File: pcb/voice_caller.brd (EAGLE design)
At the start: 52.4 x 59.1 mm, 36 parts, among them IC1 PRO_MICRO, IC3 78L12SMD, K1 TQ2SA-L2-5V, U1 25F32006WSOI

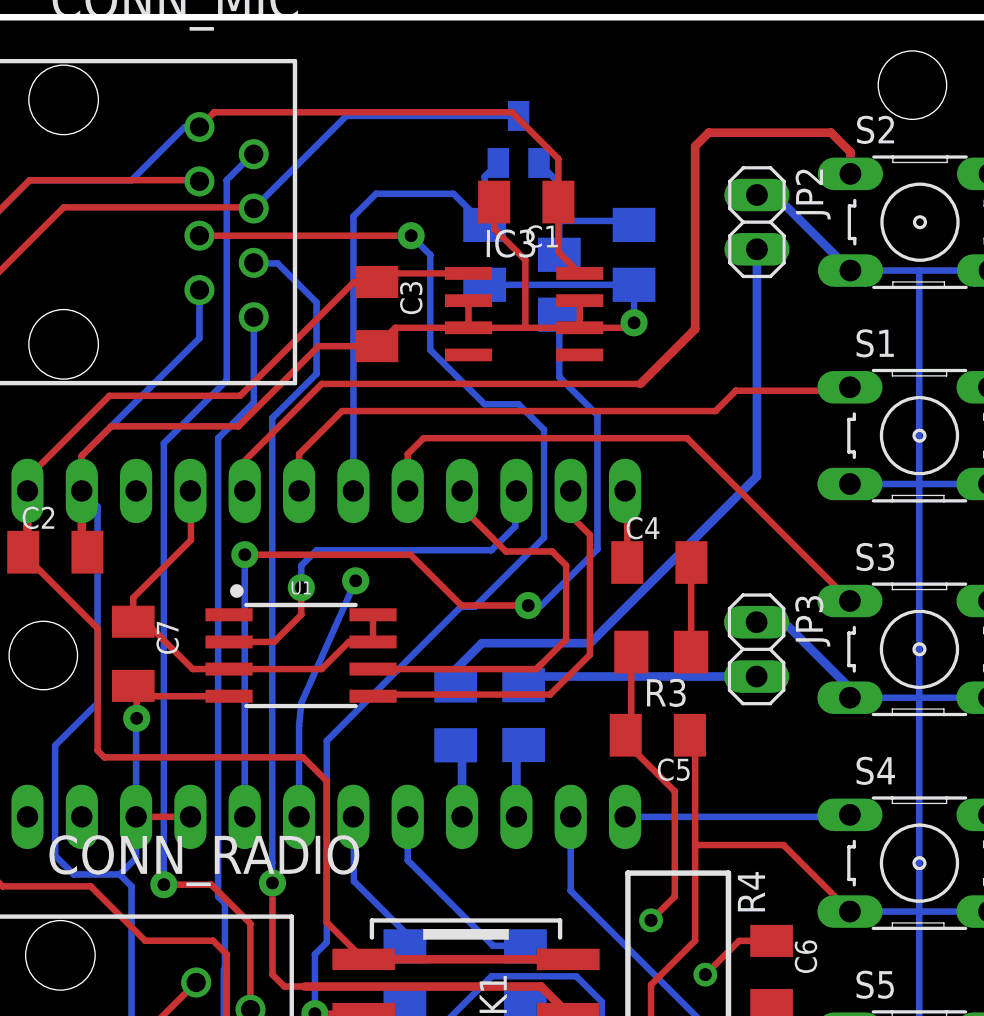
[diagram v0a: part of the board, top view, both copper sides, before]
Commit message: Flash routed, PTT sense changed.
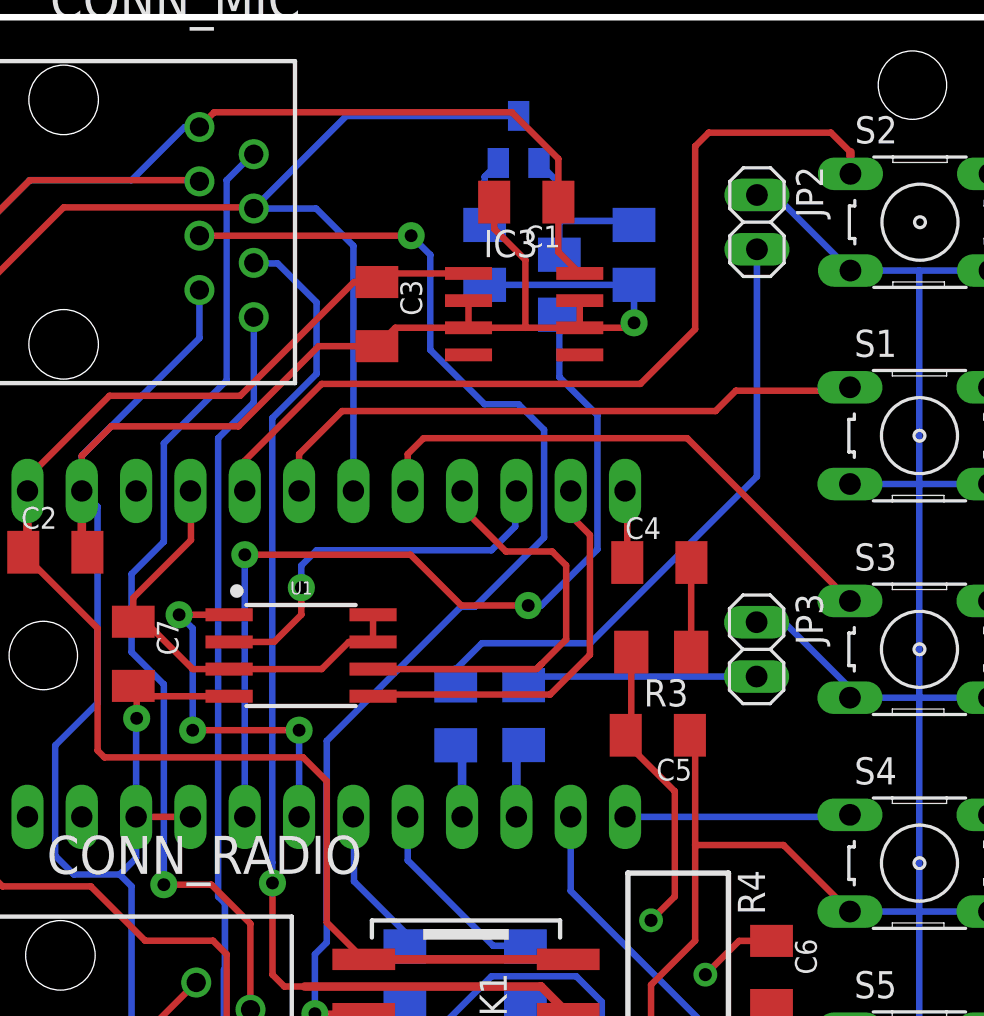
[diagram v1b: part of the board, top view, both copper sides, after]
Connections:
- net PTT: now also IC1.18
- net PTT_SENSE: no longer IC1.18
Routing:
- net PTT_SENSE: track 23.2 -> 3.16 mm
- net PTT: track 73.9 -> 90.8 mm
- net FLASH_CS: track 11.6 -> 17.0 mm, vias 1 -> 3
- net FREQ_UD: track 44.8 -> 46.0 mm
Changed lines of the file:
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@@
 <contactref element="JP3" pad="1"/>
 <wire x1="48.5925" y1="36.4825" x2="49.8775" y2="36.4825" width="0.4064" layer="16"/>
-<wire x1="49.8775" y1="36.4825" x2="53.0225" y2="33.3375" width="0.4064" layer="16"/>
+<wire x1="49.8775" y1="36.4825" x2="53.0225" y2="33.3375" width="0.3048" layer="16"/>
 <wire x1="53.0225" y1="33.3375" x2="53.0225" y2="33.01900625" width="0.4064" layer="16"/>
 <wire x1="53.0225" y1="33.01900625" x2="52.957234375" y2="32.953740625" width="0.4064" layer="16"/>
 <contactref element="JP2" pad="1"/>
 <wire x1="48.6085875" y1="56.458184375" x2="49.448140625" y2="56.458184375" width="0.4064" layer="16"/>
-<wire x1="49.448140625" y1="56.458184375" x2="52.9813" y2="52.925025" width="0.4064" layer="16"/>
+<wire x1="49.448140625" y1="56.458184375" x2="52.9813" y2="52.925025" width="0.3048" layer="16"/>
 <wire x1="17.04" y1="42.62" x2="17.78" y2="41.88" width="0.3048" layer="16"/>
 <wire x1="17.78" y1="41.88" x2="17.78" y2="32.7025" width="0.3048" layer="16"/>
@@
 <signal name="FLASH_CS">
 <contactref element="IC1" pad="6"/>
-<via x="29.845" y="38.4175" extent="1-16" drill="0.6" diameter="1.27" shape="square"/>
-<wire x1="27.2" y1="27.38" x2="27.2" y2="31.645" width="0.3048" layer="16"/>
-<wire x1="27.2" y1="31.645" x2="27.305" y2="32.7025" width="0.3048" layer="16"/>
-<wire x1="27.305" y1="32.7025" x2="29.845" y2="38.4175" width="0.3048" layer="16"/>
 <contactref element="U1" pad="1"/>
-<wire x1="27.305" y1="32.7025" x2="23.9268" y2="36.83" width="0" layer="19" extent="1-16"/>
+<wire x1="23.9268" y1="36.83" x2="21.59" y2="36.83" width="0.3048" layer="1"/>
+<via x="21.59" y="36.83" extent="1-16" drill="0.6" diameter="1.27" shape="square"/>
+<via x="22.225" y="31.4325" extent="1-16" drill="0.6" diameter="1.27" shape="square"/>
+<wire x1="22.225" y1="31.4325" x2="27.2" y2="31.4325" width="0.3048" layer="1"/>
+<via x="27.2" y="31.4325" extent="1-16" drill="0.6" diameter="1.27" shape="square"/>
+<wire x1="27.2" y1="31.4325" x2="27.2" y2="27.38" width="0.3048" layer="16"/>
+<wire x1="22.225" y1="31.4325" x2="22.225" y2="36.195" width="0.3048" layer="16"/>
+<wire x1="22.225" y1="36.195" x2="21.59" y2="36.83" width="0.3048" layer="16"/>
 </signal>
 <signal name="PTT">
@@
 <wire x1="12.7" y1="52.3875" x2="16.1925" y2="55.88" width="0.3048" layer="1"/>
 <wire x1="12.7" y1="24.765" x2="13.335" y2="24.13" width="0.3048" layer="1"/>
+<contactref element="IC1" pad="18"/>
+<wire x1="29.74" y1="42.62" x2="29.74" y2="54.08" width="0.3048" layer="16"/>
+<wire x1="29.74" y1="54.08" x2="27.995" y2="55.825" width="0.3048" layer="16"/>
+<wire x1="27.995" y1="55.825" x2="25.08" y2="55.825" width="0.3048" layer="16"/>
 </signal>
 <signal name="+8V">
@@
 <contactref element="CONN_MIC" pad="2"/>
 <contactref element="CONN_RADIO" pad="2"/>
-<wire x1="20.875625" y1="24.209375" x2="20.875625" y2="44.846875" width="0.3048" layer="16"/>
 <wire x1="20.875625" y1="44.846875" x2="23.8125" y2="47.78375" width="0.3048" layer="16"/>
 <wire x1="23.8125" y1="47.78375" x2="23.8125" y2="57.15" width="0.3048" layer="16"/>
@@
 <wire x1="24.92375" y1="22.38375" x2="23.098125" y2="24.209375" width="0.3048" layer="1"/>
 <wire x1="23.098125" y1="24.209375" x2="20.875625" y2="24.209375" width="0.3048" layer="1"/>
+<wire x1="20.875625" y1="44.846875" x2="20.875625" y2="40.243125" width="0.3048" layer="16"/>
+<wire x1="20.875625" y1="40.243125" x2="19.3675" y2="38.735" width="0.3048" layer="16"/>
+<wire x1="19.3675" y1="38.735" x2="19.3675" y2="35.08375" width="0.3048" layer="16"/>
+<wire x1="20.875625" y1="24.209375" x2="20.875625" y2="33.575625" width="0.3048" layer="16"/>
+<wire x1="19.3675" y1="35.08375" x2="20.875625" y2="33.575625" width="0.3048" layer="16"/>
 </signal>
 <signal name="SQUELCH">
@@
 <wire x1="24.66" y1="42.62" x2="24.66" y2="44.0275" width="0.3048" layer="1"/>
 <wire x1="24.66" y1="44.0275" x2="28.2575" y2="47.625" width="0.3048" layer="1"/>
-<wire x1="43.160075" y1="47.625" x2="45.72" y2="50.184925" width="0.4064" layer="1"/>
-<wire x1="45.72" y1="50.184925" x2="45.72" y2="58.7375" width="0.4064" layer="1"/>
-<wire x1="45.72" y1="58.7375" x2="46.355" y2="59.3725" width="0.4064" layer="1"/>
-<wire x1="46.355" y1="59.3725" x2="52.07" y2="59.3725" width="0.4064" layer="1"/>
-<wire x1="52.07" y1="59.3725" x2="52.9813" y2="58.4612" width="0.4064" layer="1"/>
+<wire x1="43.160075" y1="47.625" x2="45.72" y2="50.184925" width="0.3048" layer="1"/>
+<wire x1="45.72" y1="50.184925" x2="45.72" y2="58.7375" width="0.3048" layer="1"/>
+<wire x1="45.72" y1="58.7375" x2="46.355" y2="59.3725" width="0.3048" layer="1"/>
+<wire x1="46.355" y1="59.3725" x2="52.07" y2="59.3725" width="0.3048" layer="1"/>
+<wire x1="52.07" y1="59.3725" x2="52.9813" y2="58.4612" width="0.3048" layer="1"/>
 <wire x1="52.9813" y1="58.4612" x2="52.9813" y2="57.446225" width="0.4064" layer="1"/>
 </signal>
@@
 <wire x1="35.8775" y1="55.0575" x2="35.8775" y2="57.3175" width="0.3048" layer="16"/>
 <wire x1="35.8775" y1="57.3175" x2="36.515" y2="57.955" width="0.3048" layer="16"/>
-<wire x1="35.8775" y1="55.0575" x2="34.42" y2="56.515" width="0.3048" layer="16"/>
-<wire x1="34.42" y1="56.515" x2="30.7975" y2="56.515" width="0.3048" layer="16"/>
-<wire x1="30.7975" y1="56.515" x2="29.74" y2="55.4575" width="0.3048" layer="16"/>
-<contactref element="IC1" pad="18"/>
-<wire x1="29.74" y1="42.62" x2="29.74" y2="55.4575" width="0.3048" layer="16"/>
 </signal>
 <signal name="BUTTON3">
@@
 <signal name="N$4">
 <contactref element="R12" pad="1"/>
-<wire x1="40.8125" y1="35.5" x2="35.75" y2="35.5" width="0.4064" layer="16"/>
-<wire x1="35.75" y1="35.5" x2="34.525" y2="34.275" width="0.4064" layer="16"/>
+<wire x1="40.8125" y1="35.5" x2="35.75" y2="35.5" width="0.3048" layer="16"/>
+<wire x1="35.75" y1="35.5" x2="34.525" y2="34.275" width="0.3048" layer="16"/>
 <wire x1="34.525" y1="34.275" x2="34.525" y2="33.525" width="0.4064" layer="16"/>
 <contactref element="JP2" pad="2"/>
-<wire x1="40.8125" y1="35.5" x2="48.6085875" y2="43.2960875" width="0.4064" layer="16"/>
-<wire x1="48.6085875" y1="43.2960875" x2="48.6085875" y2="53.918184375" width="0.4064" layer="16"/>
+<wire x1="40.8125" y1="35.5" x2="48.6085875" y2="43.2960875" width="0.3048" layer="16"/>
+<wire x1="48.6085875" y1="43.2960875" x2="48.6085875" y2="53.918184375" width="0.3048" layer="16"/>
 </signal>
 <signal name="N$9">
@@
 <wire x1="37.7" y1="33.5375" x2="38.105" y2="33.9425" width="0.4064" layer="16"/>
 <contactref element="JP3" pad="2"/>
-<wire x1="38.105" y1="33.9425" x2="48.5925" y2="33.9425" width="0.4064" layer="16"/>
+<wire x1="38.105" y1="33.9425" x2="48.5925" y2="33.9425" width="0.3048" layer="16"/>
 </signal>
 <signal name="N$12">

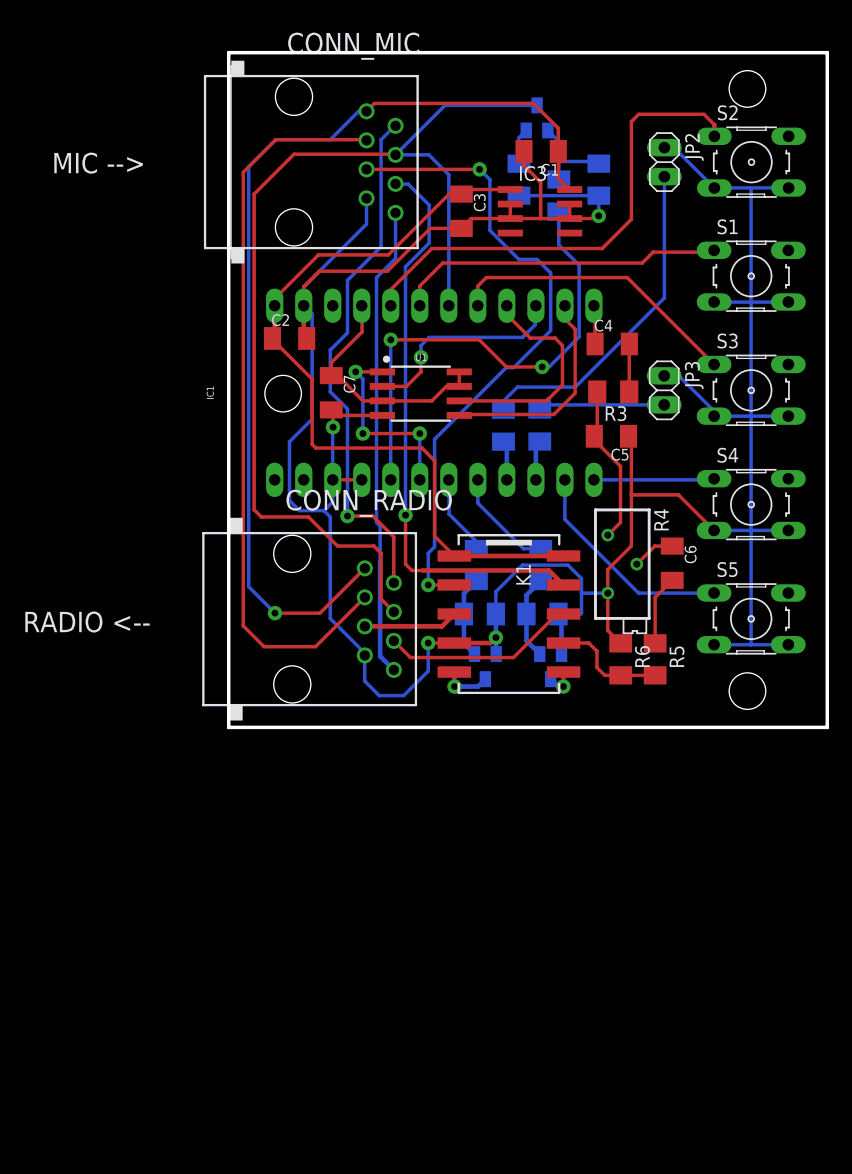
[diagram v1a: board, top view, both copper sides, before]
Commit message: Monitor amp added and routed.
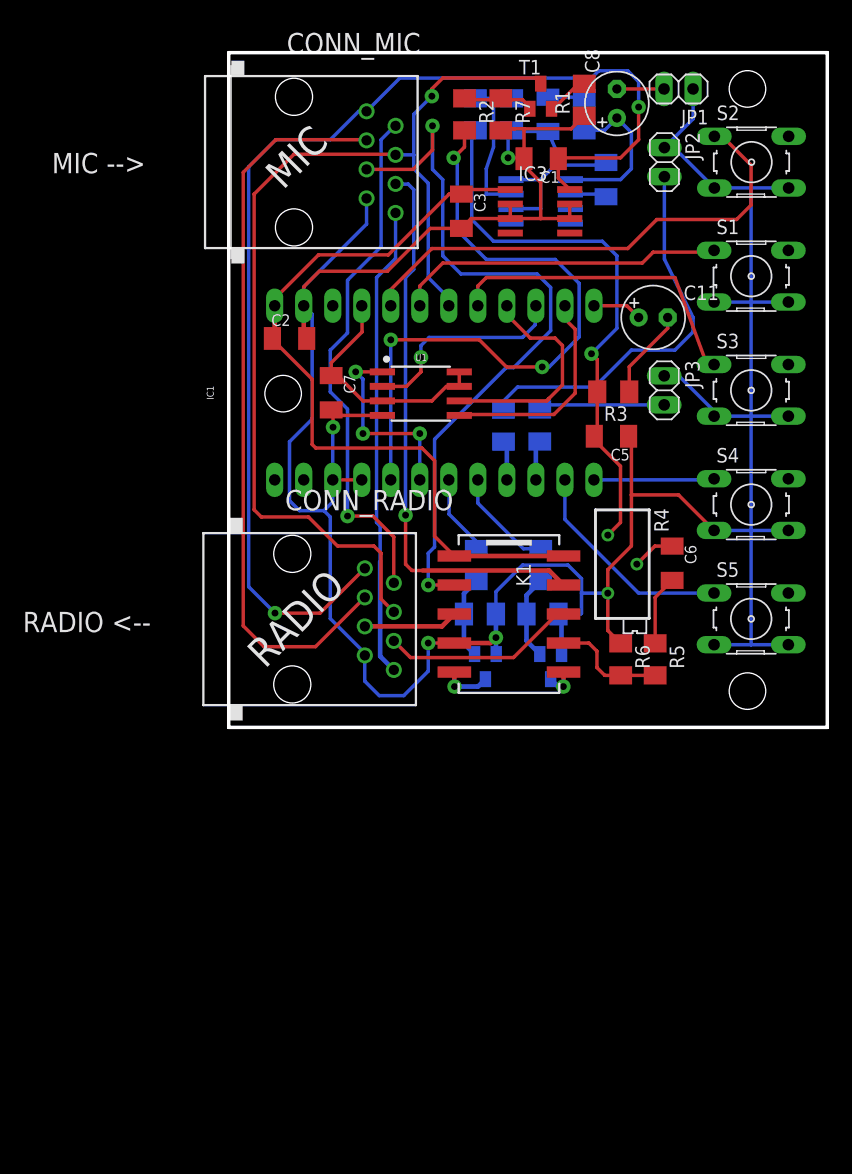
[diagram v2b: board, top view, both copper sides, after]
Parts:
- removed C4: 100uF, rcl:C1206K
- added C10, C9: 100nF, rcl:C1206K
- added C11, C8: (no value), rcl:E2,5-6
- added IC2: LM386M-1, linear:SO08
- added JP1: (no value), pinhead:1X02
- added R14, R15, R16: 220, rcl:M1206
- moved R2 10.9 mm to (31.1, 59.4), flipped to the top
- moved R7 10.3 mm to (34.3, 59.4), flipped to the top
- moved R1 9.03 mm to (41.6, 60.6), flipped to the top
- moved T1 1.93 mm to (37.8, 61.0), flipped to the top
- moved C1 0.63 mm to (37.8, 55.5)
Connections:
- new net AUDIO: C5.2, R15.2, R3.2, R4.1
- new net N$16: C8.+, IC2.5, R14.2
- new net N$21: C9.1, R14.1
- new net N$22: C8.-, JP1.2
- new net VCC: C10.1, IC2.6
- net GND: now also C10.2, C9.2, IC2.2, IC2.4, JP1.1, R16.1
- net N$1: now also C11.-; no longer C4.2
- net N$2: now also IC2.3, R15.1, R16.2; no longer C5.2, R3.2, R4.1
- net PWM: now also C11.+; no longer C4.1
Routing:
- net AUDIO: track 0.00 -> 49.1 mm, vias 0 -> 1
- net GND: track 271.8 -> 301.6 mm
- net +8V: track 85.6 -> 103.4 mm, vias 1 -> 2
- net PTT_SW: track 42.5 -> 57.4 mm, vias 2 -> 3
- net N$16: track 0.00 -> 14.0 mm
- net MIC_GND: track 56.9 -> 64.1 mm
- net N$4: track 29.2 -> 34.0 mm
- net N$22: track 0.00 -> 4.13 mm
- net VCC: track 0.00 -> 3.99 mm
- net N$1: track 4.19 -> 7.90 mm
- net N$21: track 0.00 -> 3.22 mm
- net BUTTON3: track 25.9 -> 28.0 mm
- net N$5: track 8.37 -> 6.31 mm
- net PTT: track 90.8 -> 92.4 mm, vias 0 -> 1
- net BUTTON1: track 42.5 -> 43.8 mm
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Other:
- board text added: "MIC"
- board text added: "RADIO"
